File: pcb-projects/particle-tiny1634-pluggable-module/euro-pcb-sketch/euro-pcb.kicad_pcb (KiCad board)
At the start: 2 copper layers, 157.5 x 73.7 mm, 132 parts, among them IC1 ATTINY1634-SU, P1 INTERFACE, P2 MCU_TEST

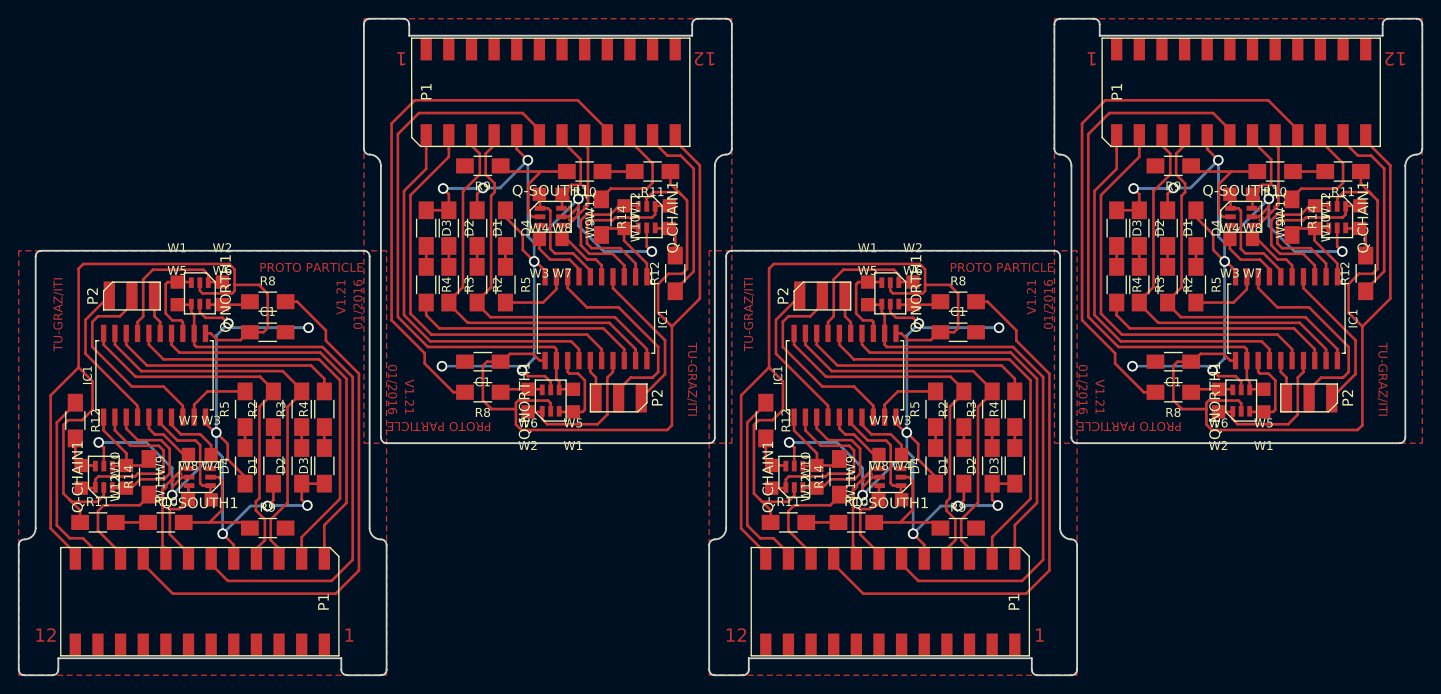
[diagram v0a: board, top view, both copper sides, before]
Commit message: change shape, updated euro pcb
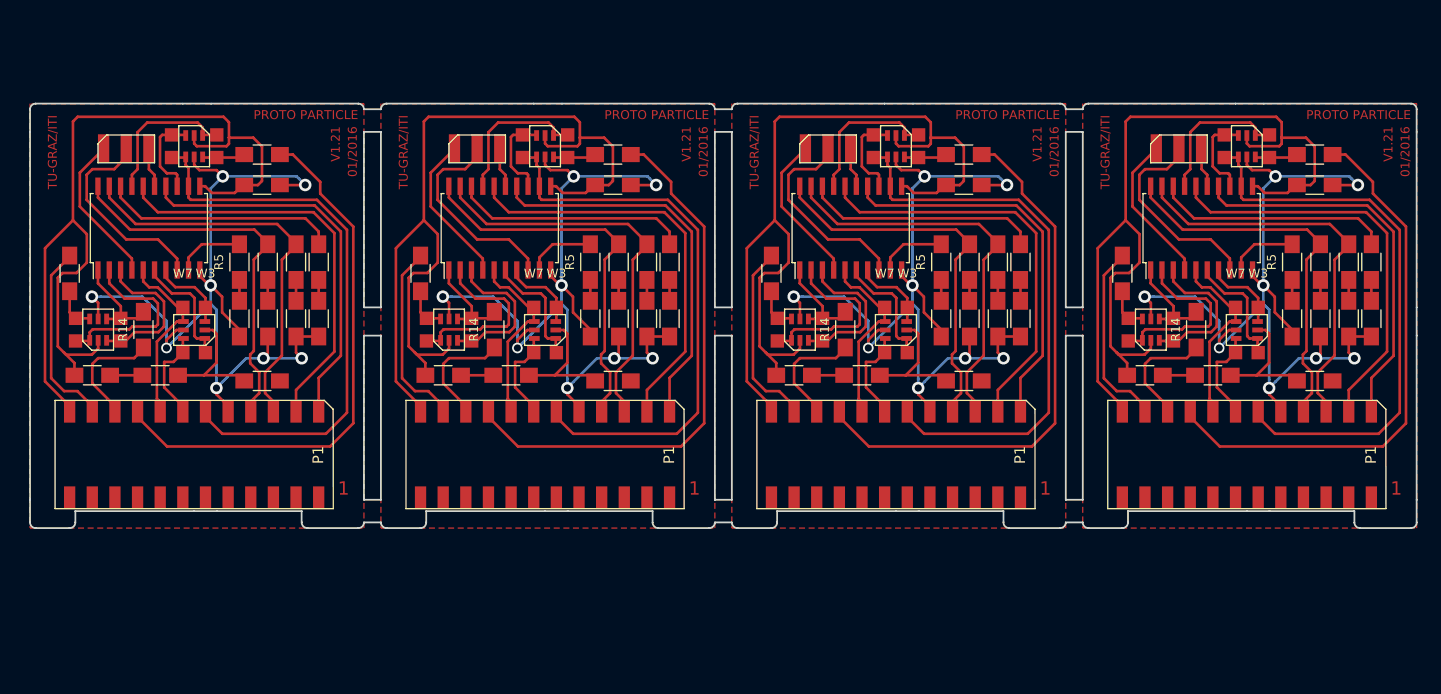
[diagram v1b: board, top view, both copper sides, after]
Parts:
- removed the C1 at (170.2, 101.9)
- removed the C1 at (194.3, 105.2)
- removed the C1 at (116.8, 105.2)
- removed the D1 at (170.8, 116.8)
- removed the D1 at (193.7, 90.2)
- removed the D1 at (116.2, 90.2)
- removed the D2 at (174.0, 116.8)
- removed the D2 at (190.5, 90.2)
- removed the D2 at (113.0, 90.2)
- removed the D3 at (176.5, 116.8)
- removed the D3 at (188.0, 90.2)
- removed the D3 at (110.5, 90.2)
- removed the D4 at (167.6, 116.8)
- removed the D4 at (196.8, 90.2)
- removed the D4 at (119.4, 90.2)
- removed the IC1 at (157.5, 106.7)
- removed the IC1 at (207.0, 100.3)
- removed the IC1 at (129.5, 100.3)
- removed the P1 at (162.6, 132.1)
- removed the P1 at (201.9, 74.9)
- removed the P1 at (124.5, 74.9)
- removed the P2 at (154.9, 97.8)
- removed the P2 at (209.6, 109.2)
- removed the P2 at (132.1, 109.2)
- removed the Q-CHAIN1 at (151.8, 118.1)
- removed the Q-CHAIN1 at (212.7, 88.9)
- removed the Q-CHAIN1 at (135.2, 88.9)
- removed the Q-NORTH1 at (201.9, 109.5)
- removed the Q-NORTH1 at (162.6, 97.5)
- removed the Q-NORTH1 at (124.5, 109.5)
- removed the Q-SOUTH1 at (162.6, 118.1)
- removed the Q-SOUTH1 at (201.9, 88.9)
- removed the Q-SOUTH1 at (124.5, 88.9)
- removed the R10 at (158.8, 123.2)
- removed the R10 at (205.7, 83.8)
- removed the R10 at (128.3, 83.8)
- removed the R11 at (151.1, 123.2)
- removed the R11 at (213.4, 83.8)
- removed the R11 at (135.9, 83.8)
- removed the R12 at (148.6, 111.8)
- removed the R12 at (215.9, 95.2)
- removed the R12 at (138.4, 95.2)
- removed the R14 at (156.9, 118.1)
- removed the R14 at (207.6, 88.9)
- removed the R14 at (130.2, 88.9)
- removed the R2 at (170.8, 110.5)
- removed the R2 at (193.7, 96.5)
- removed the R2 at (116.2, 96.5)
- removed the R3 at (174.0, 110.5)
- removed the R3 at (190.5, 96.5)
- removed the R3 at (113.0, 96.5)
- removed the R4 at (176.5, 110.5)
- removed the R4 at (188.0, 96.5)
- removed the R4 at (110.5, 96.5)
- removed the R5 at (167.6, 110.5)
- removed the R5 at (196.8, 96.5)
- removed the R5 at (119.4, 96.5)
- removed the R8 at (170.2, 98.4)
- removed the R8 at (194.3, 108.6)
- removed the R8 at (116.8, 108.6)
- removed the R9 at (170.2, 123.8)
- removed the R9 at (194.3, 83.2)
- removed the R9 at (116.8, 83.2)
- removed the W1 at (204.5, 110.8)
- removed the W1 at (160.0, 96.2)
- removed the W1 at (127.0, 110.8)
- removed the W10 at (149.2, 116.8)
- removed the W10 at (215.2, 90.2)
- removed the W10 at (137.8, 90.2)
- removed the W11 at (154.3, 119.3)
- removed the W11 at (210.2, 87.7)
- removed the W11 at (132.7, 87.7)
- removed the W12 at (149.2, 119.3)
- removed the W12 at (215.2, 87.7)
- removed the W12 at (137.8, 87.7)
- removed the W2 at (199.4, 110.8)
- removed the W2 at (165.1, 96.2)
- removed the W2 at (121.9, 110.8)
- removed the W3 at (163.8, 115.6)
- removed the W3 at (200.7, 91.4)
- removed the W3 at (123.2, 91.4)
- removed the W4 at (163.8, 120.7)
- removed the W4 at (200.7, 86.4)
- removed the W4 at (123.2, 86.4)
- removed the W5 at (204.5, 108.2)
- removed the W5 at (160.0, 98.8)
- removed the W5 at (127.0, 108.2)
- removed the W6 at (199.4, 108.2)
- removed the W6 at (165.1, 98.8)
- removed the W6 at (121.9, 108.2)
- removed the W7 at (161.3, 115.6)
- removed the W7 at (203.2, 91.4)
- removed the W7 at (125.7, 91.4)
- removed the W8 at (161.3, 120.7)
- removed the W8 at (203.2, 86.4)
- removed the W8 at (125.7, 86.4)
- removed the W9 at (154.3, 116.8)
- removed the W9 at (210.2, 90.2)
- removed the W9 at (132.7, 90.2)
- added C1: 100nF, Capacitors_SMD:C_1206_HandSoldering, F.Cu at (210.2, 85.3)
- added C1: 100nF, Capacitors_SMD:C_1206_HandSoldering, F.Cu at (170.8, 85.3)
- added C1: 100nF, Capacitors_SMD:C_1206_HandSoldering, F.Cu at (131.4, 85.3)
- added D1: HEARTBEAT, Resistors_SMD:R_1206_HandSoldering, F.Cu at (210.8, 100.3)
- added D1: HEARTBEAT, Resistors_SMD:R_1206_HandSoldering, F.Cu at (171.4, 100.3)
- added D1: HEARTBEAT, Resistors_SMD:R_1206_HandSoldering, F.Cu at (132.1, 100.3)
- added D2: STATUS0, Resistors_SMD:R_1206_HandSoldering, F.Cu at (174.6, 100.3)
- added D2: STATUS0, Resistors_SMD:R_1206_HandSoldering, F.Cu at (214.0, 100.3)
- added D2: STATUS0, Resistors_SMD:R_1206_HandSoldering, F.Cu at (135.3, 100.3)
- added D3: STATUS1, Resistors_SMD:R_1206_HandSoldering, F.Cu at (177.2, 100.3)
- added D3: STATUS1, Resistors_SMD:R_1206_HandSoldering, F.Cu at (216.5, 100.3)
- added D3: STATUS1, Resistors_SMD:R_1206_HandSoldering, F.Cu at (137.8, 100.3)
- added D4: ERROR, Resistors_SMD:R_1206_HandSoldering, F.Cu at (207.6, 100.3)
- added D4: ERROR, Resistors_SMD:R_1206_HandSoldering, F.Cu at (168.3, 100.3)
- added D4: ERROR, Resistors_SMD:R_1206_HandSoldering, F.Cu at (128.9, 100.3)
- added IC1: ATTINY1634-SU, Housings_SOIC:SOIC-20_7.5x12.8mm_Pitch1.27mm, F.Cu at (197.5, 90.2)
- added IC1: ATTINY1634-SU, Housings_SOIC:SOIC-20_7.5x12.8mm_Pitch1.27mm, F.Cu at (158.1, 90.2)
- added IC1: ATTINY1634-SU, Housings_SOIC:SOIC-20_7.5x12.8mm_Pitch1.27mm, F.Cu at (118.7, 90.2)
- added P1: INTERFACE, CONN_SMT_FCI_01x12_RIGHT_ANGLED-71607-312LF:01x12-FCI-71607-312LF, F.Cu at (202.6, 115.6)
- added P1: INTERFACE, CONN_SMT_FCI_01x12_RIGHT_ANGLED-71607-312LF:01x12-FCI-71607-312LF, F.Cu at (163.2, 115.6)
- added P1: INTERFACE, CONN_SMT_FCI_01x12_RIGHT_ANGLED-71607-312LF:01x12-FCI-71607-312LF, F.Cu at (123.8, 115.6)
- added P2: MCU_TEST, SMT_PIN_HEADER:CONN-1x3, F.Cu at (194.9, 81.3)
- added P2: MCU_TEST, SMT_PIN_HEADER:CONN-1x3, F.Cu at (155.6, 81.3)
- added P2: MCU_TEST, SMT_PIN_HEADER:CONN-1x3, F.Cu at (116.2, 81.3)
- added Q-CHAIN1: DMC2700UDM-7, sot26:SOT-26, F.Cu at (191.8, 101.6)
- added Q-CHAIN1: DMC2700UDM-7, sot26:SOT-26, F.Cu at (152.4, 101.6)
- added Q-CHAIN1: DMC2700UDM-7, sot26:SOT-26, F.Cu at (113.1, 101.6)
- added Q-NORTH1: DMC2700UDM-7, sot26:SOT-26, F.Cu at (202.6, 81.0)
- added Q-NORTH1: DMC2700UDM-7, sot26:SOT-26, F.Cu at (163.2, 81.0)
- added Q-NORTH1: DMC2700UDM-7, sot26:SOT-26, F.Cu at (123.8, 81.0)
- added Q-SOUTH1: DMC2700UDM-7, sot26:SOT-26, F.Cu at (202.6, 101.6)
- added Q-SOUTH1: DMC2700UDM-7, sot26:SOT-26, F.Cu at (163.2, 101.6)
- added Q-SOUTH1: DMC2700UDM-7, sot26:SOT-26, F.Cu at (123.8, 101.6)
- added R10: 0R, Resistors_SMD:R_1206_HandSoldering, F.Cu at (198.8, 106.7)
- added R10: 0R, Resistors_SMD:R_1206_HandSoldering, F.Cu at (159.4, 106.7)
- added R10: 0R, Resistors_SMD:R_1206_HandSoldering, F.Cu at (120.0, 106.7)
- added R11: 0R, Resistors_SMD:R_1206_HandSoldering, F.Cu at (191.1, 106.7)
- added R11: 0R, Resistors_SMD:R_1206_HandSoldering, F.Cu at (151.8, 106.7)
- added R11: 0R, Resistors_SMD:R_1206_HandSoldering, F.Cu at (112.4, 106.7)
- added R12: 1k2, Resistors_SMD:R_1206_HandSoldering, F.Cu at (188.6, 95.2)
- added R12: 1k2, Resistors_SMD:R_1206_HandSoldering, F.Cu at (149.2, 95.2)
- added R12: 1k2, Resistors_SMD:R_1206_HandSoldering, F.Cu at (109.9, 95.2)
- added R14: 0R, Resistors_SMD:R_1206_HandSoldering, F.Cu at (196.9, 101.6)
- added R14: 0R, Resistors_SMD:R_1206_HandSoldering, F.Cu at (157.5, 101.6)
- added R14: 0R, Resistors_SMD:R_1206_HandSoldering, F.Cu at (118.1, 101.6)
- added R2: 1k2, Resistors_SMD:R_1206_HandSoldering, F.Cu at (210.8, 94.0)
- added R2: 1k2, Resistors_SMD:R_1206_HandSoldering, F.Cu at (171.4, 94.0)
- added R2: 1k2, Resistors_SMD:R_1206_HandSoldering, F.Cu at (132.1, 94.0)
- added R3: 1k2, Resistors_SMD:R_1206_HandSoldering, F.Cu at (214.0, 94.0)
- added R3: 1k2, Resistors_SMD:R_1206_HandSoldering, F.Cu at (174.6, 94.0)
- added R3: 1k2, Resistors_SMD:R_1206_HandSoldering, F.Cu at (135.3, 94.0)
- added R4: 1k2, Resistors_SMD:R_1206_HandSoldering, F.Cu at (216.5, 94.0)
- added R4: 1k2, Resistors_SMD:R_1206_HandSoldering, F.Cu at (177.2, 94.0)
- added R4: 1k2, Resistors_SMD:R_1206_HandSoldering, F.Cu at (137.8, 94.0)
- added R5: 1k2, Resistors_SMD:R_1206_HandSoldering, F.Cu at (207.6, 94.0)
- added R5: 1k2, Resistors_SMD:R_1206_HandSoldering, F.Cu at (168.3, 94.0)
- added R5: 1k2, Resistors_SMD:R_1206_HandSoldering, F.Cu at (128.9, 94.0)
- added R8: 0R, Resistors_SMD:R_1206_HandSoldering, F.Cu at (210.2, 81.9)
- added R8: 0R, Resistors_SMD:R_1206_HandSoldering, F.Cu at (170.8, 81.9)
- added R8: 0R, Resistors_SMD:R_1206_HandSoldering, F.Cu at (131.4, 81.9)
- added R9: 0R, Resistors_SMD:R_1206_HandSoldering, F.Cu at (210.2, 107.3)
- added R9: 0R, Resistors_SMD:R_1206_HandSoldering, F.Cu at (170.8, 107.3)
- added R9: 0R, Resistors_SMD:R_1206_HandSoldering, F.Cu at (131.4, 107.3)
- added W1: TP1-N, Measurement_Points:Measurement_Point_Square-SMD-Pad_Small, F.Cu at (200.0, 79.7)
- added W1: TP1-N, Measurement_Points:Measurement_Point_Square-SMD-Pad_Small, F.Cu at (160.7, 79.7)
- added W1: TP1-N, Measurement_Points:Measurement_Point_Square-SMD-Pad_Small, F.Cu at (121.3, 79.7)
- added W10: TP3-C, Measurement_Points:Measurement_Point_Square-SMD-Pad_Small, F.Cu at (189.3, 100.3)
- added W10: TP3-C, Measurement_Points:Measurement_Point_Square-SMD-Pad_Small, F.Cu at (149.9, 100.3)
- added W10: TP3-C, Measurement_Points:Measurement_Point_Square-SMD-Pad_Small, F.Cu at (110.5, 100.3)
- added W11: TP2-C, Measurement_Points:Measurement_Point_Square-SMD-Pad_Small, F.Cu at (194.3, 102.8)
- added W11: TP2-C, Measurement_Points:Measurement_Point_Square-SMD-Pad_Small, F.Cu at (155.0, 102.8)
- added W11: TP2-C, Measurement_Points:Measurement_Point_Square-SMD-Pad_Small, F.Cu at (115.6, 102.8)
- added W12: TP4-C, Measurement_Points:Measurement_Point_Square-SMD-Pad_Small, F.Cu at (189.3, 102.8)
- added W12: TP4-C, Measurement_Points:Measurement_Point_Square-SMD-Pad_Small, F.Cu at (149.9, 102.8)
- added W12: TP4-C, Measurement_Points:Measurement_Point_Square-SMD-Pad_Small, F.Cu at (110.5, 102.8)
- added W2: TP3-N, Measurement_Points:Measurement_Point_Square-SMD-Pad_Small, F.Cu at (205.1, 79.7)
- added W2: TP3-N, Measurement_Points:Measurement_Point_Square-SMD-Pad_Small, F.Cu at (165.7, 79.7)
- added W2: TP3-N, Measurement_Points:Measurement_Point_Square-SMD-Pad_Small, F.Cu at (126.4, 79.7)
- added W3: TP1-S, Measurement_Points:Measurement_Point_Square-SMD-Pad_Small, F.Cu at (203.8, 99.1)
- added W3: TP1-S, Measurement_Points:Measurement_Point_Square-SMD-Pad_Small, F.Cu at (164.5, 99.1)
- added W3: TP1-S, Measurement_Points:Measurement_Point_Square-SMD-Pad_Small, F.Cu at (125.1, 99.1)
- added W4: TP3-S, Measurement_Points:Measurement_Point_Square-SMD-Pad_Small, F.Cu at (203.8, 104.1)
- added W4: TP3-S, Measurement_Points:Measurement_Point_Square-SMD-Pad_Small, F.Cu at (164.5, 104.1)
- added W4: TP3-S, Measurement_Points:Measurement_Point_Square-SMD-Pad_Small, F.Cu at (125.1, 104.1)
- added W5: TP2-N, Measurement_Points:Measurement_Point_Square-SMD-Pad_Small, F.Cu at (200.0, 82.2)
- added W5: TP2-N, Measurement_Points:Measurement_Point_Square-SMD-Pad_Small, F.Cu at (160.7, 82.2)
- added W5: TP2-N, Measurement_Points:Measurement_Point_Square-SMD-Pad_Small, F.Cu at (121.3, 82.2)
- added W6: TP4-N, Measurement_Points:Measurement_Point_Square-SMD-Pad_Small, F.Cu at (205.1, 82.2)
- added W6: TP4-N, Measurement_Points:Measurement_Point_Square-SMD-Pad_Small, F.Cu at (165.7, 82.2)
- added W6: TP4-N, Measurement_Points:Measurement_Point_Square-SMD-Pad_Small, F.Cu at (126.4, 82.2)
- added W7: TP2-S, Measurement_Points:Measurement_Point_Square-SMD-Pad_Small, F.Cu at (201.3, 99.1)
- added W7: TP2-S, Measurement_Points:Measurement_Point_Square-SMD-Pad_Small, F.Cu at (161.9, 99.1)
- added W7: TP2-S, Measurement_Points:Measurement_Point_Square-SMD-Pad_Small, F.Cu at (122.6, 99.1)
- added W8: TP4-S, Measurement_Points:Measurement_Point_Square-SMD-Pad_Small, F.Cu at (201.3, 104.1)
- added W8: TP4-S, Measurement_Points:Measurement_Point_Square-SMD-Pad_Small, F.Cu at (161.9, 104.1)
- added W8: TP4-S, Measurement_Points:Measurement_Point_Square-SMD-Pad_Small, F.Cu at (122.6, 104.1)
- added W9: TP1-C, Measurement_Points:Measurement_Point_Square-SMD-Pad_Small, F.Cu at (194.3, 100.3)
- added W9: TP1-C, Measurement_Points:Measurement_Point_Square-SMD-Pad_Small, F.Cu at (155.0, 100.3)
- added W9: TP1-C, Measurement_Points:Measurement_Point_Square-SMD-Pad_Small, F.Cu at (115.6, 100.3)
- moved P1 16.5 mm to (84.5, 115.6)
- moved C1 16.5 mm to (92.1, 85.3)
- moved D1 16.5 mm to (92.7, 100.3)
- moved D2 16.5 mm to (95.9, 100.3)
- moved D3 16.5 mm to (98.4, 100.3)
- moved D4 16.5 mm to (89.5, 100.3)
- moved IC1 16.5 mm to (79.4, 90.2)
- moved P2 16.5 mm to (76.8, 81.3)
- moved Q-CHAIN1 16.5 mm to (73.7, 101.6)
- moved Q-SOUTH1 16.5 mm to (84.5, 101.6)
- moved R12 16.5 mm to (70.5, 95.2)
- moved R14 16.5 mm to (78.8, 101.6)
- moved R9 16.5 mm to (92.1, 107.3)
- moved W1 16.5 mm to (81.9, 79.7)
- moved W10 16.5 mm to (71.1, 100.3)
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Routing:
- net GND: track 381.8 -> 394.9 mm
- net /RX-SOUTH: track 80.5 -> 77.6 mm
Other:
- board size 157.5 x 73.7 mm -> 155.6 x 47.6 mm
- net class Default: via_dia 1.2 -> 1.4
- board text removed: "12"
